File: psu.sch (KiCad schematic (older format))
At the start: 9 parts

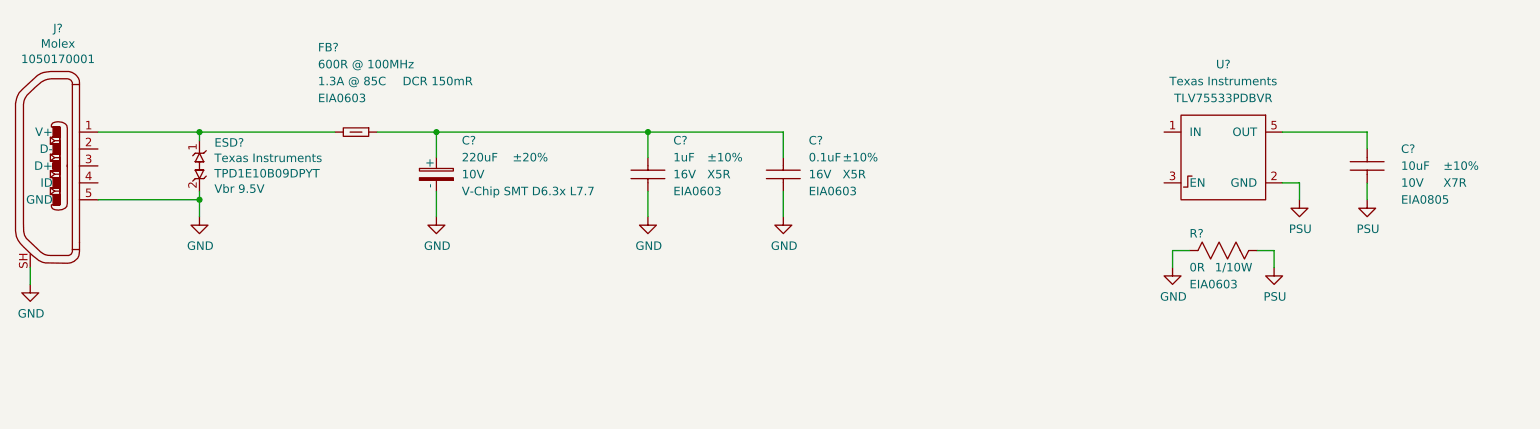
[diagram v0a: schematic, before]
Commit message: Add filter cap to LDO EN pin.
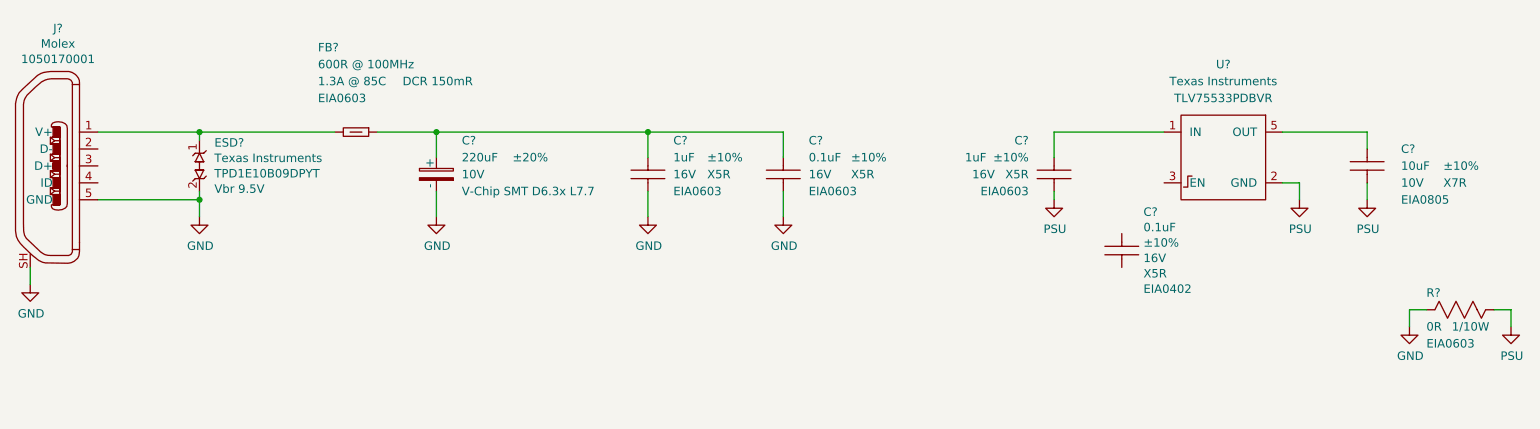
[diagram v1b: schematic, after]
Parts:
- added C?: CAP-EIA0603, footprints_generic:CAPC160X80X95L35N, symbol gz_Ceramic-Capacitors:CAP-EIA0603
- added C?: CAP-EIA0402, footprints_generic:CAPC100X50X55L30N, symbol gz_Ceramic-Capacitors:CAP-EIA0402
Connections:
- net GND: now also C?.2
- net at U?.1 (IN): now also C?.1
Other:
- moved on the sheet: R?
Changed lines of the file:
@@
 F 8 "Ceramic Capacitors" H 2500 6800 50  0001 L CNN "Family"
 F 9 "0.1uF" V 5700 2100 50  0000 L CNN "Capacitance"
-F 10 "±10%" V 5700 2300 50  0000 L CNN "Tolerance"
+F 10 "±10%" V 5700 2350 50  0000 L CNN "Tolerance"
 F 11 "16V" V 5800 2100 50  0000 L CNN "Voltage"
-F 12 "X5R" V 5800 2300 50  0000 L CNN "Dielectric"
+F 12 "X5R" V 5800 2350 50  0000 L CNN "Dielectric"
 F 13 "EIA0603" V 5900 2100 50  0000 L CNN "Package"
 	1    5800 1950
@@
 L gz_Power-Symbols:PSU #PWR?
 U 1 1 6046A224
-P 8700 2500
-F 0 "#PWR?" H 8700 2250 50  0001 C CNN
-F 1 "PSU" H 8705 2327 50  0000 C CNN
-F 2 "" H 8700 2500 50  0001 C CNN
-F 3 "" H 8700 2500 50  0001 C CNN
-	1    8700 2500
+P 10100 2850
+F 0 "#PWR?" H 10100 2600 50  0001 C CNN
+F 1 "PSU" H 10105 2677 50  0000 C CNN
+F 2 "" H 10100 2850 50  0001 C CNN
+F 3 "" H 10100 2850 50  0001 C CNN
+	1    10100 2850
 	1    0    0    -1
 $EndComp
@@
 L gz_Power-Symbols:GND #PWR?
 U 1 1 6046B337
-P 8100 2500
-F 0 "#PWR?" H 8100 2250 50  0001 C CNN
-F 1 "GND" H 8105 2327 50  0000 C CNN
-F 2 "" H 8100 2500 50  0001 C CNN
-F 3 "" H 8100 2500 50  0001 C CNN
-	1    8100 2500
+P 9500 2850
+F 0 "#PWR?" H 9500 2600 50  0001 C CNN
+F 1 "GND" H 9505 2677 50  0000 C CNN
+F 2 "" H 9500 2850 50  0001 C CNN
+F 3 "" H 9500 2850 50  0001 C CNN
+	1    9500 2850
 	1    0    0    -1
 $EndComp
@@
 L gz_Chip-Resistors-Surface-Mount:RES-EIA0603 R?
 U 1 1 6046C6CC
-P 8400 2400
-F 0 "R?" H 8200 2500 50  0000 L CNN
-F 1 "RES-EIA0603" H 9200 3300 50  0001 L CNN
-F 2 "footprints_generic:RESC160X85X55L30N" H 5100 6750 50  0001 L CNN
-F 3 "http://industrial.panasonic.com/www-cgi/jvcr13pz.cgi?E+PZ+3+AOA0001+ERJ3GEY0R00V+7+WW" H 5100 6850 50  0001 L CNN
-F 4 "P0.0GCT-ND" H 9200 3200 50  0001 L CNN "Digi-Key_PN"
-F 5 "Panasonic Electronic Components" H 9200 3100 50  0001 L CNN "Manufacturer"
-F 6 "ERJ-3GEY0R00V" H 9200 3000 50  0001 L CNN "MPN"
-F 7 "Resistors" H 5100 7150 50  0001 L CNN "Category"
-F 8 "Chip Resistor - Surface Mount" H 5100 7250 50  0001 L CNN "Family"
-F 9 "0R" H 8200 2300 50  0000 L CNN "Resistance"
-F 10 "N/A" H 8400 2797 50  0001 L CNN "Tolerance"
-F 11 "1/10W" H 8350 2300 50  0000 L CNN "Power"
-F 12 "N/A" H 8400 2615 50  0001 L CNN "Voltage"
-F 13 "EIA0603" H 8200 2200 50  0000 L CNN "Package"
-	1    8400 2400
-	1    0    0    -1
-$EndComp
-Wire Wire Line
-	8100 2500 8100 2400
-Wire Wire Line
-	8100 2400 8200 2400
-Wire Wire Line
-	8600 2400 8700 2400
-Wire Wire Line
-	8700 2400 8700 2500
+P 9800 2750
+F 0 "R?" H 9600 2850 50  0000 L CNN
+F 1 "RES-EIA0603" H 10600 3650 50  0001 L CNN
+F 2 "footprints_generic:RESC160X85X55L30N" H 6500 7100 50  0001 L CNN
+F 3 "http://industrial.panasonic.com/www-cgi/jvcr13pz.cgi?E+PZ+3+AOA0001+ERJ3GEY0R00V+7+WW" H 6500 7200 50  0001 L CNN
+F 4 "P0.0GCT-ND" H 10600 3550 50  0001 L CNN "Digi-Key_PN"
+F 5 "Panasonic Electronic Components" H 10600 3450 50  0001 L CNN "Manufacturer"
+F 6 "ERJ-3GEY0R00V" H 10600 3350 50  0001 L CNN "MPN"
+F 7 "Resistors" H 6500 7500 50  0001 L CNN "Category"
+F 8 "Chip Resistor - Surface Mount" H 6500 7600 50  0001 L CNN "Family"
+F 9 "0R" H 9600 2650 50  0000 L CNN "Resistance"
+F 10 "N/A" H 9800 3147 50  0001 L CNN "Tolerance"
+F 11 "1/10W" H 9750 2650 50  0000 L CNN "Power"
+F 12 "N/A" H 9800 2965 50  0001 L CNN "Voltage"
+F 13 "EIA0603" H 9600 2550 50  0000 L CNN "Package"
+	1    9800 2750
+	1    0    0    -1
+$EndComp
+Wire Wire Line
+	9500 2850 9500 2750
+Wire Wire Line
+	9500 2750 9600 2750
+Wire Wire Line
+	10000 2750 10100 2750
+Wire Wire Line
+	10100 2750 10100 2850
 Wire Wire Line
 	9250 2000 9250 2100
@@
 Wire Wire Line
 	8850 2000 8850 2100
+$Comp
+L gz_Ceramic-Capacitors:CAP-EIA0603 C?
+U 1 1 6047D273
+P 7400 1950
+F 0 "C?" V 7200 1800 50  0000 R CNN
+F 1 "CAP-EIA0603" H 7800 3050 50  0001 L CNN
+F 2 "footprints_generic:CAPC160X80X95L35N" H 4100 6300 50  0001 L CNN
+F 3 "https://api.kemet.com/component-edge/download/specsheet/C0603C105K4PAC7411.pdf" H 4100 6400 50  0001 L CNN
+F 4 "399-C0603C105K4PAC7411CT-ND" H 7800 2950 50  0001 L CNN "Digi-Key_PN"
+F 5 "KEMET" H 7800 2850 50  0001 L CNN "Manufacturer"
+F 6 "C0603C105K4PAC7411" H 7800 2750 50  0001 L CNN "MPN"
+F 7 "Capacitors" H 4100 6700 50  0001 L CNN "Category"
+F 8 "Ceramic Capacitors" H 4100 6800 50  0001 L CNN "Family"
+F 9 "1uF" V 7300 1550 50  0000 R CNN "Capacitance"
+F 10 "±10%" V 7300 1800 50  0000 R CNN "Tolerance"
+F 11 "16V" V 7400 1600 50  0000 R CNN "Voltage"
+F 12 "X5R" V 7400 1800 50  0000 R CNN "Dielectric"
+F 13 "EIA0603" V 7500 1800 50  0000 R CNN "Package"
+	1    7400 1950
+	0    1    1    0
+$EndComp
+Wire Wire Line
+	8050 1700 7400 1700
+Wire Wire Line
+	7400 1700 7400 1850
+Wire Wire Line
+	7400 2050 7400 2100
+$Comp
+L gz_Power-Symbols:PSU #PWR?
+U 1 1 6047F48F
+P 7400 2100
+F 0 "#PWR?" H 7400 1850 50  0001 C CNN
+F 1 "PSU" H 7405 1927 50  0000 C CNN
+F 2 "" H 7400 2100 50  0001 C CNN
+F 3 "" H 7400 2100 50  0001 C CNN
+	1    7400 2100
+	1    0    0    -1
+$EndComp
+$Comp
+L gz_Ceramic-Capacitors:CAP-EIA0402 C?
+U 1 1 60483D8C
+P 7800 2400
+F 0 "C?" V 7572 2528 50  0000 L CNN
+F 1 "CAP-EIA0402" H 8200 3500 50  0001 L CNN
+F 2 "footprints_generic:CAPC100X50X55L30N" H 4500 6750 50  0001 L CNN
+F 3 "https://api.kemet.com/component-edge/download/datasheet/C0402C104K4PACTU.pdf" H 4500 6850 50  0001 L CNN
+F 4 "399-7762-1-ND" H 8200 3400 50  0001 L CNN "Digi-Key_PN"
+F 5 "KEMET" H 8200 3300 50  0001 L CNN "Manufacturer"
+F 6 "C0402C104K4PACTU" H 8200 3200 50  0001 L CNN "MPN"
+F 7 "Capacitors" H 4500 7150 50  0001 L CNN "Category"
+F 8 "Ceramic Capacitors" H 4500 7250 50  0001 L CNN "Family"
+F 9 "0.1uF" V 7663 2528 50  0000 L CNN "Capacitance"
+F 10 "±10%" V 7754 2528 50  0000 L CNN "Tolerance"
+F 11 "16V" V 7845 2528 50  0000 L CNN "Voltage"
+F 12 "X5R" V 7936 2528 50  0000 L CNN "Dielectric"
+F 13 "EIA0402" V 8027 2528 50  0000 L CNN "Package"
+	1    7800 2400
+	0    1    1    0
+$EndComp
 $EndSCHEMATC

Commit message: Add PU to LDO EN line.
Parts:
- added R?: RES-EIA0402, footprints_generic:RESC100X50X40L25NN, symbol gz_Chip-Resistors-Surface-Mount:RES-EIA0402
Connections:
- net GND: now also C?.2
- net +3V3: now reaches C?.1, C?.1, C?.1 (+), FB?.2
- net +3V3: now also C?.1, U?.1 (IN), R?.2
- net at U?.3 (EN): now also C?.1, R?.1
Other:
- moved on the sheet: C?, R?
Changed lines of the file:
@@
 L gz_Power-Symbols:PSU #PWR?
 U 1 1 6046A224
-P 10100 2850
-F 0 "#PWR?" H 10100 2600 50  0001 C CNN
-F 1 "PSU" H 10105 2677 50  0000 C CNN
-F 2 "" H 10100 2850 50  0001 C CNN
-F 3 "" H 10100 2850 50  0001 C CNN
-	1    10100 2850
+P 8750 2400
+F 0 "#PWR?" H 8750 2150 50  0001 C CNN
+F 1 "PSU" H 8755 2227 50  0000 C CNN
+F 2 "" H 8750 2400 50  0001 C CNN
+F 3 "" H 8750 2400 50  0001 C CNN
+	1    8750 2400
 	1    0    0    -1
 $EndComp
@@
 L gz_Power-Symbols:GND #PWR?
 U 1 1 6046B337
-P 9500 2850
-F 0 "#PWR?" H 9500 2600 50  0001 C CNN
-F 1 "GND" H 9505 2677 50  0000 C CNN
-F 2 "" H 9500 2850 50  0001 C CNN
-F 3 "" H 9500 2850 50  0001 C CNN
-	1    9500 2850
+P 8150 2400
+F 0 "#PWR?" H 8150 2150 50  0001 C CNN
+F 1 "GND" H 8155 2227 50  0000 C CNN
+F 2 "" H 8150 2400 50  0001 C CNN
+F 3 "" H 8150 2400 50  0001 C CNN
+	1    8150 2400
 	1    0    0    -1
 $EndComp
@@
 L gz_Chip-Resistors-Surface-Mount:RES-EIA0603 R?
 U 1 1 6046C6CC
-P 9800 2750
-F 0 "R?" H 9600 2850 50  0000 L CNN
-F 1 "RES-EIA0603" H 10600 3650 50  0001 L CNN
-F 2 "footprints_generic:RESC160X85X55L30N" H 6500 7100 50  0001 L CNN
-F 3 "http://industrial.panasonic.com/www-cgi/jvcr13pz.cgi?E+PZ+3+AOA0001+ERJ3GEY0R00V+7+WW" H 6500 7200 50  0001 L CNN
-F 4 "P0.0GCT-ND" H 10600 3550 50  0001 L CNN "Digi-Key_PN"
-F 5 "Panasonic Electronic Components" H 10600 3450 50  0001 L CNN "Manufacturer"
-F 6 "ERJ-3GEY0R00V" H 10600 3350 50  0001 L CNN "MPN"
-F 7 "Resistors" H 6500 7500 50  0001 L CNN "Category"
-F 8 "Chip Resistor - Surface Mount" H 6500 7600 50  0001 L CNN "Family"
-F 9 "0R" H 9600 2650 50  0000 L CNN "Resistance"
-F 10 "N/A" H 9800 3147 50  0001 L CNN "Tolerance"
-F 11 "1/10W" H 9750 2650 50  0000 L CNN "Power"
-F 12 "N/A" H 9800 2965 50  0001 L CNN "Voltage"
-F 13 "EIA0603" H 9600 2550 50  0000 L CNN "Package"
-	1    9800 2750
-	1    0    0    -1
-$EndComp
-Wire Wire Line
-	9500 2850 9500 2750
-Wire Wire Line
-	9500 2750 9600 2750
-Wire Wire Line
-	10000 2750 10100 2750
-Wire Wire Line
-	10100 2750 10100 2850
+P 8450 2300
+F 0 "R?" H 8250 2400 50  0000 L CNN
+F 1 "RES-EIA0603" H 9250 3200 50  0001 L CNN
+F 2 "footprints_generic:RESC160X85X55L30N" H 5150 6650 50  0001 L CNN
+F 3 "http://industrial.panasonic.com/www-cgi/jvcr13pz.cgi?E+PZ+3+AOA0001+ERJ3GEY0R00V+7+WW" H 5150 6750 50  0001 L CNN
+F 4 "P0.0GCT-ND" H 9250 3100 50  0001 L CNN "Digi-Key_PN"
+F 5 "Panasonic Electronic Components" H 9250 3000 50  0001 L CNN "Manufacturer"
+F 6 "ERJ-3GEY0R00V" H 9250 2900 50  0001 L CNN "MPN"
+F 7 "Resistors" H 5150 7050 50  0001 L CNN "Category"
+F 8 "Chip Resistor - Surface Mount" H 5150 7150 50  0001 L CNN "Family"
+F 9 "0R" H 8250 2200 50  0000 L CNN "Resistance"
+F 10 "N/A" H 8450 2697 50  0001 L CNN "Tolerance"
+F 11 "1/10W" H 8400 2200 50  0000 L CNN "Power"
+F 12 "N/A" H 8450 2515 50  0001 L CNN "Voltage"
+F 13 "EIA0603" H 8250 2100 50  0000 L CNN "Package"
+	1    8450 2300
+	1    0    0    -1
+$EndComp
+Wire Wire Line
+	8150 2400 8150 2300
+Wire Wire Line
+	8150 2300 8250 2300
+Wire Wire Line
+	8650 2300 8750 2300
+Wire Wire Line
+	8750 2300 8750 2400
 Wire Wire Line
 	9250 2000 9250 2100
@@
 Wire Wire Line
 	8850 2000 8850 2100
+$Comp
+L gz_Ceramic-Capacitors:CAP-EIA0402 C?
+U 1 1 60483D8C
+P 7850 2950
+F 0 "C?" V 7700 3100 50  0000 L CNN
+F 1 "CAP-EIA0402" H 8250 4050 50  0001 L CNN
+F 2 "footprints_generic:CAPC100X50X55L30N" H 4550 7300 50  0001 L CNN
+F 3 "https://api.kemet.com/component-edge/download/datasheet/C0402C104K4PACTU.pdf" H 4550 7400 50  0001 L CNN
+F 4 "399-7762-1-ND" H 8250 3950 50  0001 L CNN "Digi-Key_PN"
+F 5 "KEMET" H 8250 3850 50  0001 L CNN "Manufacturer"
+F 6 "C0402C104K4PACTU" H 8250 3750 50  0001 L CNN "MPN"
+F 7 "Capacitors" H 4550 7700 50  0001 L CNN "Category"
+F 8 "Ceramic Capacitors" H 4550 7800 50  0001 L CNN "Family"
+F 9 "0.1uF" V 7800 3100 50  0000 L CNN "Capacitance"
+F 10 "±10%" V 7800 3350 50  0000 L CNN "Tolerance"
+F 11 "16V" V 7900 3100 50  0000 L CNN "Voltage"
+F 12 "X5R" V 7900 3350 50  0000 L CNN "Dielectric"
+F 13 "EIA0402" V 8000 3100 50  0000 L CNN "Package"
+	1    7850 2950
+	0    1    1    0
+$EndComp
+$Comp
+L gz_Chip-Resistors-Surface-Mount:RES-EIA0402 R?
+U 1 1 60486E18
+P 7450 2750
+F 0 "R?" H 7550 2550 50  0000 L CNN
+F 1 "RES-EIA0402" H 8250 3650 50  0001 L CNN
+F 2 "footprints_generic:RESC100X50X40L25NN" H 4150 7100 50  0001 L CNN
+F 3 "https://industrial.panasonic.com/ww/products/resistors/chip-resistors/general-purpose-chip-resistors/models/ERJ2GEJ562X" H 4150 7200 50  0001 L CNN
+F 4 "P5.6KJCT-ND" H 8250 3550 50  0001 L CNN "Digi-Key_PN"
+F 5 "Panasonic Electronic Components" H 8250 3450 50  0001 L CNN "Manufacturer"
+F 6 "ERJ-2GEJ562X" H 8250 3350 50  0001 L CNN "MPN"
+F 7 "Resistors" H 4150 7500 50  0001 L CNN "Category"
+F 8 "Chip Resistor - Surface Mount" H 4150 7600 50  0001 L CNN "Family"
+F 9 "5.6k" H 7500 2650 50  0000 L CNN "Resistance"
+F 10 "±5%" H 7300 2650 50  0000 L CNN "Tolerance"
+F 11 "1/10W" H 7400 2850 50  0000 L CNN "Power"
+F 12 "50V" V 7586 2828 50  0001 L CNN "Voltage"
+F 13 "EIA0402" H 7350 2950 50  0000 L CNN "Package"
+	1    7450 2750
+	-1   0    0    1
+$EndComp
+$Comp
+L gz_Power-Symbols:PSU #PWR?
+U 1 1 6047F48F
+P 7400 2100
+F 0 "#PWR?" H 7400 1850 50  0001 C CNN
+F 1 "PSU" H 7405 1927 50  0000 C CNN
+F 2 "" H 7400 2100 50  0001 C CNN
+F 3 "" H 7400 2100 50  0001 C CNN
+	1    7400 2100
+	1    0    0    -1
+$EndComp
+Wire Wire Line
+	7400 2050 7400 2100
+Wire Wire Line
+	7400 1700 7400 1850
+Wire Wire Line
+	8050 1700 7400 1700
 $Comp
 L gz_Ceramic-Capacitors:CAP-EIA0603 C?
@@
 $EndComp
 Wire Wire Line
-	8050 1700 7400 1700
-Wire Wire Line
-	7400 1700 7400 1850
-Wire Wire Line
-	7400 2050 7400 2100
-$Comp
-L gz_Power-Symbols:PSU #PWR?
-U 1 1 6047F48F
-P 7400 2100
-F 0 "#PWR?" H 7400 1850 50  0001 C CNN
-F 1 "PSU" H 7405 1927 50  0000 C CNN
-F 2 "" H 7400 2100 50  0001 C CNN
-F 3 "" H 7400 2100 50  0001 C CNN
-	1    7400 2100
-	1    0    0    -1
-$EndComp
-$Comp
-L gz_Ceramic-Capacitors:CAP-EIA0402 C?
-U 1 1 60483D8C
-P 7800 2400
-F 0 "C?" V 7572 2528 50  0000 L CNN
-F 1 "CAP-EIA0402" H 8200 3500 50  0001 L CNN
-F 2 "footprints_generic:CAPC100X50X55L30N" H 4500 6750 50  0001 L CNN
-F 3 "https://api.kemet.com/component-edge/download/datasheet/C0402C104K4PACTU.pdf" H 4500 6850 50  0001 L CNN
-F 4 "399-7762-1-ND" H 8200 3400 50  0001 L CNN "Digi-Key_PN"
-F 5 "KEMET" H 8200 3300 50  0001 L CNN "Manufacturer"
-F 6 "C0402C104K4PACTU" H 8200 3200 50  0001 L CNN "MPN"
-F 7 "Capacitors" H 4500 7150 50  0001 L CNN "Category"
-F 8 "Ceramic Capacitors" H 4500 7250 50  0001 L CNN "Family"
-F 9 "0.1uF" V 7663 2528 50  0000 L CNN "Capacitance"
-F 10 "±10%" V 7754 2528 50  0000 L CNN "Tolerance"
-F 11 "16V" V 7845 2528 50  0000 L CNN "Voltage"
-F 12 "X5R" V 7936 2528 50  0000 L CNN "Dielectric"
-F 13 "EIA0402" V 8027 2528 50  0000 L CNN "Package"
-	1    7800 2400
-	0    1    1    0
-$EndComp
+	7850 2750 7850 2850
+Wire Wire Line
+	7850 3050 7850 3150
+$Comp
+L gz_Power-Symbols:PSU #PWR?
+U 1 1 604A90DD
+P 7850 3150
+F 0 "#PWR?" H 7850 2900 50  0001 C CNN
+F 1 "PSU" H 7855 2977 50  0000 C CNN
+F 2 "" H 7850 3150 50  0001 C CNN
+F 3 "" H 7850 3150 50  0001 C CNN
+	1    7850 3150
+	1    0    0    -1
+$EndComp
+Wire Wire Line
+	7850 2750 7650 2750
+$Comp
+L gz_Power-Symbols:5V #PWR?
+U 1 1 604B29D2
+P 5800 1600
+F 0 "#PWR?" H 5950 1550 50  0001 C CNN
+F 1 "5V" H 5805 1723 50  0000 C CNN
+F 2 "" H 5800 1600 50  0001 C CNN
+F 3 "" H 5800 1600 50  0001 C CNN
+	1    5800 1600
+	1    0    0    -1
+$EndComp
+Wire Wire Line
+	5800 1600 5800 1700
+Connection ~ 5800 1700
+$Comp
+L gz_Power-Symbols:5V #PWR?
+U 1 1 604B3F53
+P 7400 1600
+F 0 "#PWR?" H 7550 1550 50  0001 C CNN
+F 1 "5V" H 7405 1723 50  0000 C CNN
+F 2 "" H 7400 1600 50  0001 C CNN
+F 3 "" H 7400 1600 50  0001 C CNN
+	1    7400 1600
+	1    0    0    -1
+$EndComp
+Wire Wire Line
+	7400 1600 7400 1700
+Connection ~ 7400 1700
+$Comp
+L gz_Power-Symbols:5V #PWR?
+U 1 1 604B506C
+P 7100 2650
+F 0 "#PWR?" H 7250 2600 50  0001 C CNN
+F 1 "5V" H 7105 2773 50  0000 C CNN
+F 2 "" H 7100 2650 50  0001 C CNN
+F 3 "" H 7100 2650 50  0001 C CNN
+	1    7100 2650
+	1    0    0    -1
+$EndComp
+Wire Wire Line
+	7100 2650 7100 2750
+Wire Wire Line
+	7100 2750 7250 2750
+Wire Wire Line
+	8050 2000 7850 2000
+Wire Wire Line
+	7850 2000 7850 2750
+Connection ~ 7850 2750
 $EndSCHEMATC

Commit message: Add 3V3 label to LDO output.
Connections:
- net +3V3: now also C?.1, U?.5 (OUT)
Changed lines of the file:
@@
 	7850 2000 7850 2750
 Connection ~ 7850 2750
+$Comp
+L gz_Power-Symbols:3V3 #PWR?
+U 1 1 604C2C38
+P 9250 1600
+F 0 "#PWR?" H 9400 1550 50  0001 C CNN
+F 1 "3V3" H 9255 1723 50  0000 C CNN
+F 2 "" H 9250 1600 50  0001 C CNN
+F 3 "" H 9250 1600 50  0001 C CNN
+	1    9250 1600
+	1    0    0    -1
+$EndComp
+Wire Wire Line
+	9250 1600 9250 1700
+Connection ~ 9250 1700
 $EndSCHEMATC

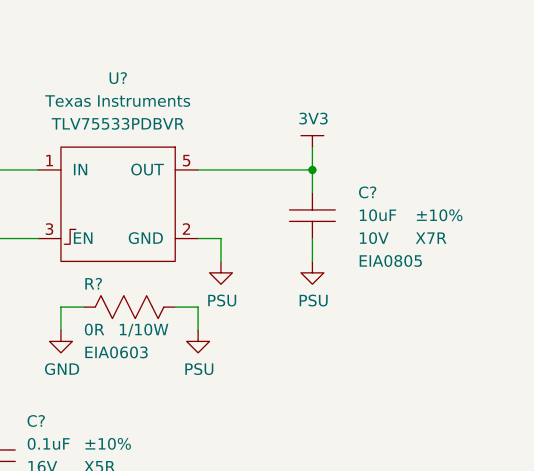
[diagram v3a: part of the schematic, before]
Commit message: Add 0R jumper to LDO output and move 3V3 label after it.
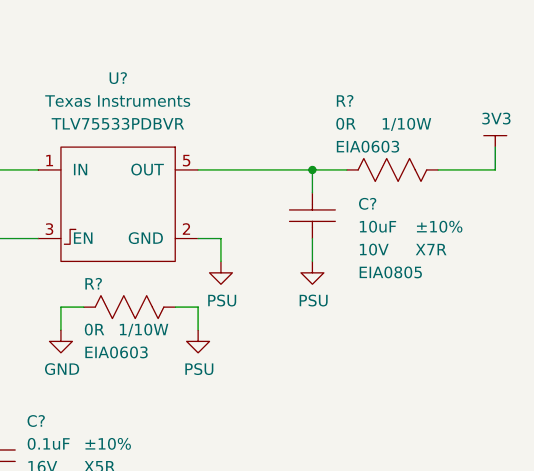
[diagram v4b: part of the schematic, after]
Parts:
- added R?: RES-EIA0603, footprints_generic:RESC160X85X55L30N, symbol gz_Chip-Resistors-Surface-Mount:RES-EIA0603
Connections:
- net +3V3: now also R?.2; no longer C?.1, U?.5 (OUT)
- new net: C?.1, R?.1, U?.5 (OUT)
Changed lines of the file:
@@
 U 1 1 6046210B
 P 9250 1900
-F 0 "C?" V 9150 2100 50  0000 L CNN
+F 0 "C?" V 9200 2100 50  0000 L CNN
 F 1 "CAP-EIA0805" H 9650 3000 50  0001 L CNN
 F 2 "footprints_generic:CAPC200X125X110L50N" H 5950 6250 50  0001 L CNN
@@
 F 7 "Capacitors" H 5950 6650 50  0001 L CNN "Category"
 F 8 "Ceramic Capacitors" H 5950 6750 50  0001 L CNN "Family"
-F 9 "10uF" V 9250 2100 50  0000 L CNN "Capacitance"
-F 10 "±10%" V 9250 2350 50  0000 L CNN "Tolerance"
-F 11 "10V" V 9350 2100 50  0000 L CNN "Voltage"
-F 12 "X7R" V 9350 2350 50  0000 L CNN "Dielectric"
-F 13 "EIA0805" V 9450 2100 50  0000 L CNN "Package"
+F 9 "10uF" V 9300 2100 50  0000 L CNN "Capacitance"
+F 10 "±10%" V 9300 2350 50  0000 L CNN "Tolerance"
+F 11 "10V" V 9400 2100 50  0000 L CNN "Voltage"
+F 12 "X7R" V 9400 2350 50  0000 L CNN "Dielectric"
+F 13 "EIA0805" V 9500 2100 50  0000 L CNN "Package"
 	1    9250 1900
 	0    1    1    0
@@
 L gz_Power-Symbols:3V3 #PWR?
 U 1 1 604C2C38
-P 9250 1600
-F 0 "#PWR?" H 9400 1550 50  0001 C CNN
-F 1 "3V3" H 9255 1723 50  0000 C CNN
-F 2 "" H 9250 1600 50  0001 C CNN
-F 3 "" H 9250 1600 50  0001 C CNN
-	1    9250 1600
-	1    0    0    -1
-$EndComp
-Wire Wire Line
-	9250 1600 9250 1700
+P 10050 1600
+F 0 "#PWR?" H 10200 1550 50  0001 C CNN
+F 1 "3V3" H 10055 1723 50  0000 C CNN
+F 2 "" H 10050 1600 50  0001 C CNN
+F 3 "" H 10050 1600 50  0001 C CNN
+	1    10050 1600
+	1    0    0    -1
+$EndComp
 Connection ~ 9250 1700
+$Comp
+L gz_Chip-Resistors-Surface-Mount:RES-EIA0603 R?
+U 1 1 604C57AE
+P 9600 1700
+F 0 "R?" H 9350 2000 50  0000 L CNN
+F 1 "RES-EIA0603" H 10400 2600 50  0001 L CNN
+F 2 "footprints_generic:RESC160X85X55L30N" H 6300 6050 50  0001 L CNN
+F 3 "http://industrial.panasonic.com/www-cgi/jvcr13pz.cgi?E+PZ+3+AOA0001+ERJ3GEY0R00V+7+WW" H 6300 6150 50  0001 L CNN
+F 4 "P0.0GCT-ND" H 10400 2500 50  0001 L CNN "Digi-Key_PN"
+F 5 "Panasonic Electronic Components" H 10400 2400 50  0001 L CNN "Manufacturer"
+F 6 "ERJ-3GEY0R00V" H 10400 2300 50  0001 L CNN "MPN"
+F 7 "Resistors" H 6300 6450 50  0001 L CNN "Category"
+F 8 "Chip Resistor - Surface Mount" H 6300 6550 50  0001 L CNN "Family"
+F 9 "0R" H 9350 1900 50  0000 L CNN "Resistance"
+F 10 "N/A" H 9600 2097 50  0001 L CNN "Tolerance"
+F 11 "1/10W" H 9550 1900 50  0000 L CNN "Power"
+F 12 "N/A" H 9600 1915 50  0001 L CNN "Voltage"
+F 13 "EIA0603" H 9350 1800 50  0000 L CNN "Package"
+	1    9600 1700
+	1    0    0    -1
+$EndComp
+Wire Wire Line
+	9250 1700 9400 1700
+Wire Wire Line
+	9800 1700 10050 1700
+Wire Wire Line
+	10050 1700 10050 1600
 $EndSCHEMATC
